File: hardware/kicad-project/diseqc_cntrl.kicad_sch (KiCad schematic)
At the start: 33 parts, among them IC1 LMR36520ADDAR, IC2 LMR36520ADDAR, J1 Barrel Jack

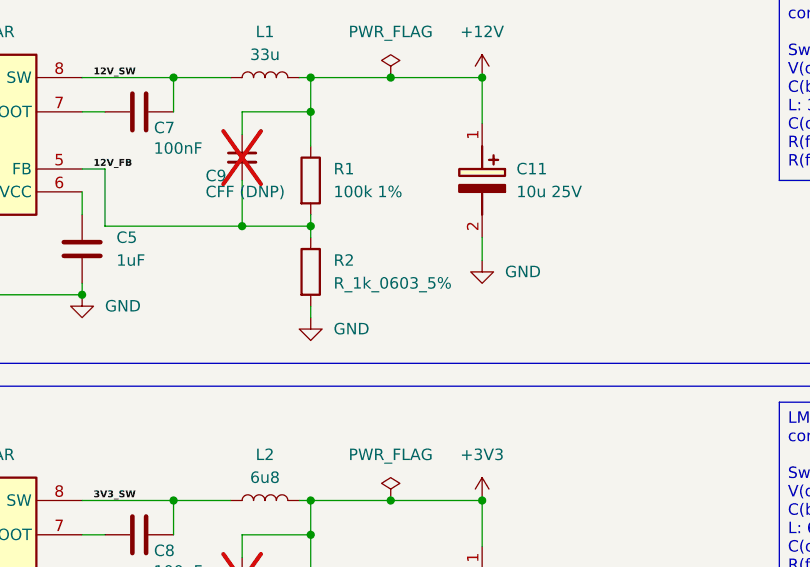
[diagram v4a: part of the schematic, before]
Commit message: Added LNB Fault pull-up and LED
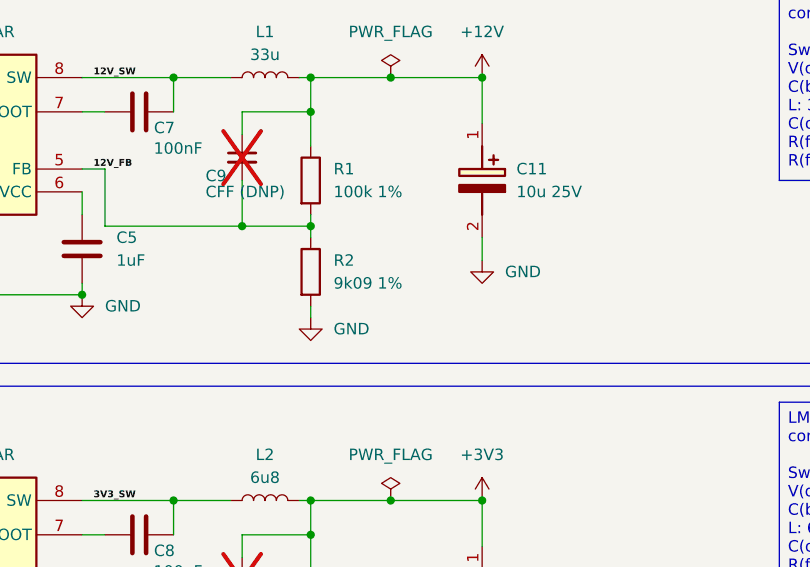
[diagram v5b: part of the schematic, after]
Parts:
- removed R2: R_1k_0603_5%, Resistor_SMD:R_0603_1608Metric_Pad0.98x0.95mm_HandSolder, symbol #InvenTree:R_1k_0603_5%
- added R2: 9k09 1%, Resistor_SMD:R_0603_1608Metric, symbol #InvenTree:R_9k09_0603_1%
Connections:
- net 12V_FB: now also R2.1
- net GND: now also R2.2
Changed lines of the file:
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@@
-	)
-	(symbol
-		(lib_id "#InvenTree:R_1k_0603_5%")
-		(at 120.65 105.41 0)
-		(unit 1)
-		(body_style 1)
-		(exclude_from_sim no)
-		(in_bom yes)
-		(on_board yes)
-		(in_pos_files yes)
-		(dnp no)
-		(fields_autoplaced yes)
-		(property "Reference" "R2"
-			(at 123.19 104.1399 0)
-			(show_name no)
-			(do_not_autoplace no)
-			(effects
-				(font
-					(size 1.27 1.27)
-				)
-				(justify left)
-			)
-		)
-		(property "Value" "R_1k_0603_5%"
-			(at 123.19 106.6799 0)
-			(show_name no)
-			(do_not_autoplace no)
-			(effects
-				(font
-					(size 1.27 1.27)
-				)
-				(justify left)
-			)
-		)
-		(property "Footprint" "Resistor_SMD:R_0603_1608Metric_Pad0.98x0.95mm_HandSolder"
-			(at 118.872 105.41 90)
-			(hide yes)
-			(show_name no)
-			(do_not_autoplace no)
-			(effects
-				(font
-					(size 1.27 1.27)
-				)
-			)
-		)
-		(property "Datasheet" "https://www.mouser.co.uk/datasheet/3/508/1/PYu-RC_Group_51_RoHS_L_12.pdf"
-			(at 120.65 105.41 0)
-			(hide yes)
-			(show_name no)
-			(do_not_autoplace no)
-			(effects
-				(font
-					(size 1.27 1.27)
-				)
-			)
-		)
-		(property "Description" "Resistor"
-			(at 120.65 105.41 0)
-			(hide yes)
-			(show_name no)
-			(do_not_autoplace no)
-			(effects
-				(font
-					(size 1.27 1.27)
-				)
-			)
-		)
-		(property "Maufacturer_Part_Number" ""
-			(at 120.65 105.41 0)
-			(hide yes)
-			(show_name no)
-			(do_not_autoplace no)
-			(effects
-				(font
-					(size 1.27 1.27)
-				)
-			)
-		)
-		(property "Manufacturer_Part_Code" ""
-			(at 120.65 105.41 0)
-			(hide yes)
-			(show_name no)
-			(do_not_autoplace no)
-			(effects
-				(font
-					(size 1.27 1.27)
-				)
-			)
-		)
-		(property "Mouser_Part_Number" ""
-			(at 120.65 105.41 0)
-			(hide yes)
-			(show_name no)
-			(do_not_autoplace no)
-			(effects
-				(font
-					(size 1.27 1.27)
-				)
-			)
-		)
-		(property "Mouser Part Number" "603-RC0603FR-1322K1L"
-			(at 120.65 105.41 0)
-			(hide yes)
-			(show_name no)
-			(do_not_autoplace no)
-			(effects
-				(font
-					(size 1.27 1.27)
-				)
-			)
-		)
-		(property "InvenTree Part" "R_22k1_0603_1%"
-			(at 120.65 105.41 0)
-			(hide yes)
-			(show_name no)
-			(do_not_autoplace no)
-			(effects
-				(font
-					(size 1.27 1.27)
-				)
-			)
-		)
-		(property "KLC_S4.2_3V3OUT" ""
-			(at 120.65 105.41 0)
-			(hide yes)
-			(show_name no)
-			(do_not_autoplace no)
-			(effects
-				(font
-					(size 1.27 1.27)
-				)
-			)
-		)
-		(property "KLC_S4.2_VCC" ""
-			(at 120.65 105.41 0)
-			(hide yes)
-			(show_name no)
-			(do_not_autoplace no)
-			(effects
-				(font
-					(size 1.27 1.27)
-				)
-			)
-		)
-		(property "Tolerance" "5%"
-			(at 120.65 105.41 0)
-			(hide yes)
-			(show_name no)
-			(do_not_autoplace no)
-			(effects
-				(font
-					(size 1.27 1.27)
-				)
-			)
-		)
-		(property "InvenTree" "176"
-			(at 120.65 105.41 0)
-			(hide yes)
-			(show_name no)
-			(do_not_autoplace no)
-			(effects
-				(font
-					(size 1.27 1.27)
-				)
-			)
-		)
-		(property "ToleranceRequirement" "<=1%"
-			(at 120.65 105.41 0)
-			(hide yes)
-			(show_name no)
-			(do_not_autoplace no)
-			(effects
-				(font
-					(size 1.27 1.27)
-				)
-			)
-		)
-		(property "Part URL" "https://inventree.ebnx.net/web/part/176/"
-			(at 120.65 105.41 0)
-			(hide yes)
-			(show_name no)
-			(do_not_autoplace no)
-			(effects
-				(font
-					(size 1.27 1.27)
-				)
-			)
-		)
-		(pin "1"
-		)
-		(pin "2"
-		)
-		(instances
-			(project "diseqc_cntrl"
-				(path "/82a905d8-f1d7-4995-9c16-94cf3cdcaad9"
-					(reference "R2")
-					(unit 1)
-				)
-			)
-		)
 	)
 	(symbol
@@
 					(unit 1)
 				)
+			)
+		)
+	)
+	(symbol
+		(lib_id "#InvenTree:R_9k09_0603_1%")
+		(at 120.65 105.41 0)
+		(unit 1)
+		(body_style 1)
+		(exclude_from_sim no)
+		(in_bom yes)
+		(on_board yes)
+		(in_pos_files yes)
+		(dnp no)
+		(fields_autoplaced yes)
+		(property "Reference" "R2"
+			(at 123.19 104.1399 0)
+			(show_name no)
+			(do_not_autoplace no)
+			(effects
+				(font
+					(size 1.27 1.27)
+				)
+				(justify left)
+			)
+		)
+		(property "Value" "9k09 1%"
+			(at 123.19 106.6799 0)
+			(show_name no)
+			(do_not_autoplace no)
+			(effects
+				(font
+					(size 1.27 1.27)
+				)
+				(justify left)
+			)
+		)
+		(property "Footprint" "Resistor_SMD:R_0603_1608Metric"
+			(at 118.872 105.41 90)
+			(hide yes)
+			(show_name no)
+			(do_not_autoplace no)
+			(effects
+				(font
+					(size 1.27 1.27)
+				)
+			)
+		)
+		(property "Datasheet" ""
+			(at 120.65 105.41 0)
+			(hide yes)
+			(show_name no)
+			(do_not_autoplace no)
+			(effects
+				(font
+					(size 1.27 1.27)
+				)
+			)
+		)
+		(property "Description" ""
+			(at 120.65 105.41 0)
+			(hide yes)
+			(show_name no)
+			(do_not_autoplace no)
+			(effects
+				(font
+					(size 1.27 1.27)
+				)
+			)
+		)
+		(property "InvenTree" "265"
+			(at 120.65 105.41 0)
+			(hide yes)
+			(show_name no)
+			(do_not_autoplace no)
+			(effects
+				(font
+					(size 1.27 1.27)
+				)
+			)
+		)
+		(property "Part URL" "https://inventree.ebnx.net/web/part/265/"
+			(at 120.65 105.41 0)
+			(hide yes)
+			(show_name no)
+			(do_not_autoplace no)
+			(effects
+				(font
+					(size 1.27 1.27)
+				)
+			)
+		)
+		(pin "1"
+		)
+		(pin "2"
+		)
+		(instances
+			(project "diseqc_cntrl"
+				(path "/82a905d8-f1d7-4995-9c16-94cf3cdcaad9"
+					(reference "R2")
+					(unit 1)
+				)

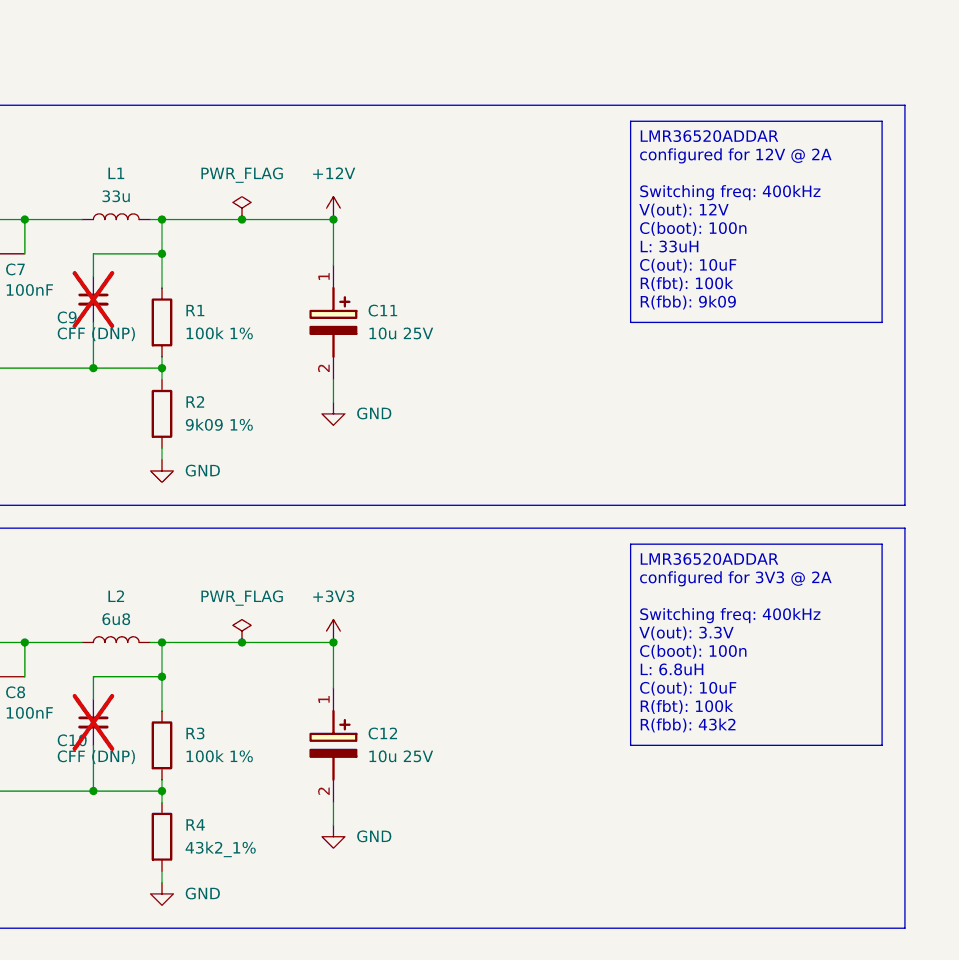
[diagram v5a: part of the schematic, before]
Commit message: Updated Vreg output caps to match datasheet
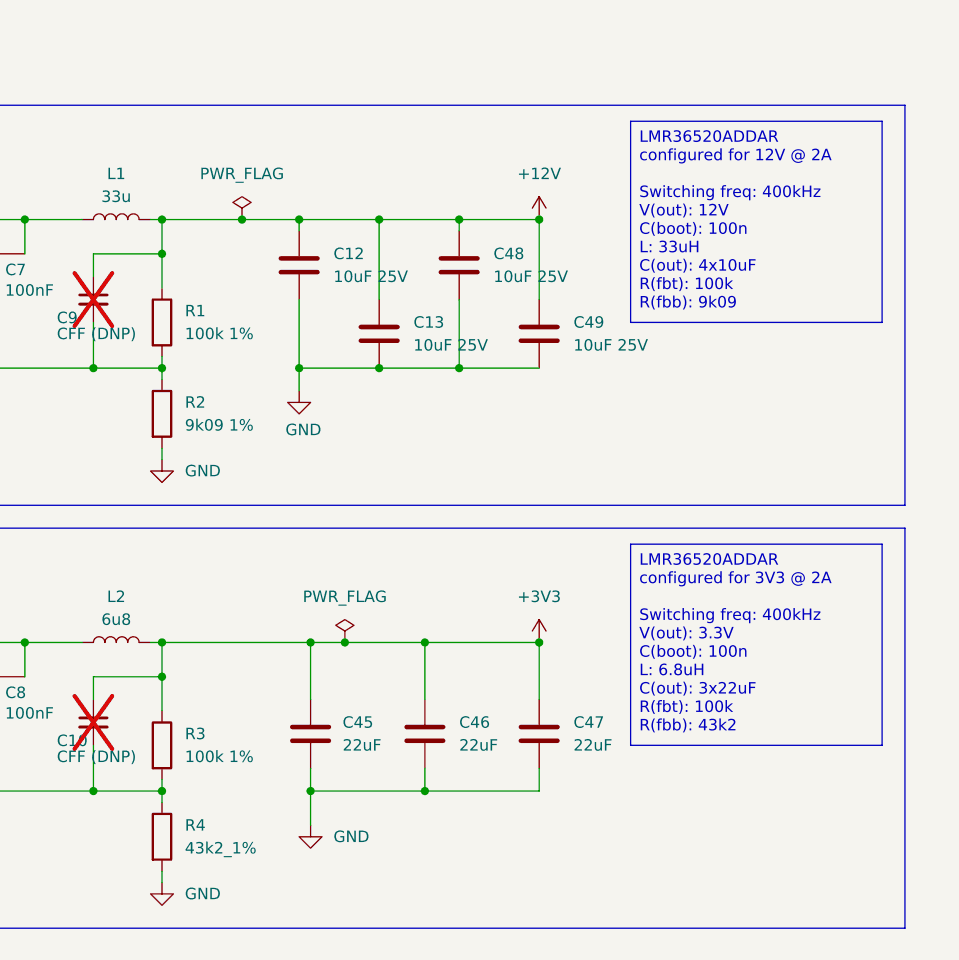
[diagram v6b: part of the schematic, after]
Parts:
- removed C11, C12: 10u 25V, CAPAE400X550N, symbol diseqc_cntrl:865080440002
- added C12, C13, C48, C49: 10uF 25V, Capacitor_SMD:C_1206_3216Metric, symbol #InvenTree:C_10uF_1206_25V
- added C45, C46, C47: 22uF, Capacitor_SMD:C_0603_1608Metric, symbol #InvenTree:C_22uF_0603_10V
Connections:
- net +12V: now also C12.1, C13.1, C48.1, C49.1
- net +3V3: now also C45.1, C46.1, C47.1
- net GND: now also C12.2, C13.2, C45.2, C46.2, C47.2, C48.2, C49.2

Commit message: Add fiducials
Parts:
- added FID1, FID2, FID3: Fiducial, Fiducial:Fiducial_1mm_Mask2mm, symbol Mechanical:Fiducial
- renumbered C12 to C11, C45 to C12, C46 to C14, C48 to C15, C49 to C16, C47 to C17
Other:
- note added: "Mechanical"
